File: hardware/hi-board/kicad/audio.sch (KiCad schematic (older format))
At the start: 10 parts, among them J2 Speaker, U1 LM386

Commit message: Complete display schematic and change footprints
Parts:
- C2, C3: footprint Capacitor_SMD:C_0402_1005Metric -> Capacitor_SMD:C_0603_1608Metric
- R1, R2, R3, R4, R5: footprint Resistor_SMD:R_0402_1005Metric -> Resistor_SMD:R_0603_1608Metric
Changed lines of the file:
@@
 F 0 "R1" V 3400 2950 50  0000 C CNN
 F 1 "1k" V 3400 3150 50  0000 C CNN
-F 2 "Resistor_SMD:R_0402_1005Metric" H 3500 3050 50  0001 C CNN
+F 2 "Resistor_SMD:R_0603_1608Metric" H 3500 3050 50  0001 C CNN
 F 3 "~" H 3500 3050 50  0001 C CNN
 	1    3500 3050
@@
 F 0 "R2" V 3400 3300 50  0000 C CNN
 F 1 "1k" V 3400 3500 50  0000 C CNN
-F 2 "Resistor_SMD:R_0402_1005Metric" H 3500 3400 50  0001 C CNN
+F 2 "Resistor_SMD:R_0603_1608Metric" H 3500 3400 50  0001 C CNN
 F 3 "~" H 3500 3400 50  0001 C CNN
 	1    3500 3400
@@
 F 0 "C2" H 3992 3696 50  0000 L CNN
 F 1 "4.7nF" H 3992 3605 50  0000 L CNN
-F 2 "Capacitor_SMD:C_0402_1005Metric" H 3900 3650 50  0001 C CNN
+F 2 "Capacitor_SMD:C_0603_1608Metric" H 3900 3650 50  0001 C CNN
 F 3 "~" H 3900 3650 50  0001 C CNN
 	1    3900 3650
@@
 F 0 "R3" V 4600 3300 50  0000 C CNN
 F 1 "10k" V 4600 3500 50  0000 C CNN
-F 2 "Resistor_SMD:R_0402_1005Metric" H 4700 3400 50  0001 C CNN
+F 2 "Resistor_SMD:R_0603_1608Metric" H 4700 3400 50  0001 C CNN
 F 3 "~" H 4700 3400 50  0001 C CNN
 	1    4700 3400
@@
 F 0 "R4" H 4359 3696 50  0000 L CNN
 F 1 "4.7k" H 4359 3605 50  0000 L CNN
-F 2 "Resistor_SMD:R_0402_1005Metric" H 4300 3650 50  0001 C CNN
+F 2 "Resistor_SMD:R_0603_1608Metric" H 4300 3650 50  0001 C CNN
 F 3 "~" H 4300 3650 50  0001 C CNN
 	1    4300 3650
@@
 F 0 "C3" H 6092 3696 50  0000 L CNN
 F 1 "47nF" H 6092 3605 50  0000 L CNN
-F 2 "Capacitor_SMD:C_0402_1005Metric" H 6000 3650 50  0001 C CNN
+F 2 "Capacitor_SMD:C_0603_1608Metric" H 6000 3650 50  0001 C CNN
 F 3 "~" H 6000 3650 50  0001 C CNN
 	1    6000 3650
@@
 F 0 "R5" H 6059 3946 50  0000 L CNN
 F 1 "10Ω" H 6059 3855 50  0000 L CNN
-F 2 "Resistor_SMD:R_0402_1005Metric" H 6000 3900 50  0001 C CNN
+F 2 "Resistor_SMD:R_0603_1608Metric" H 6000 3900 50  0001 C CNN
 F 3 "~" H 6000 3900 50  0001 C CNN
 	1    6000 3900

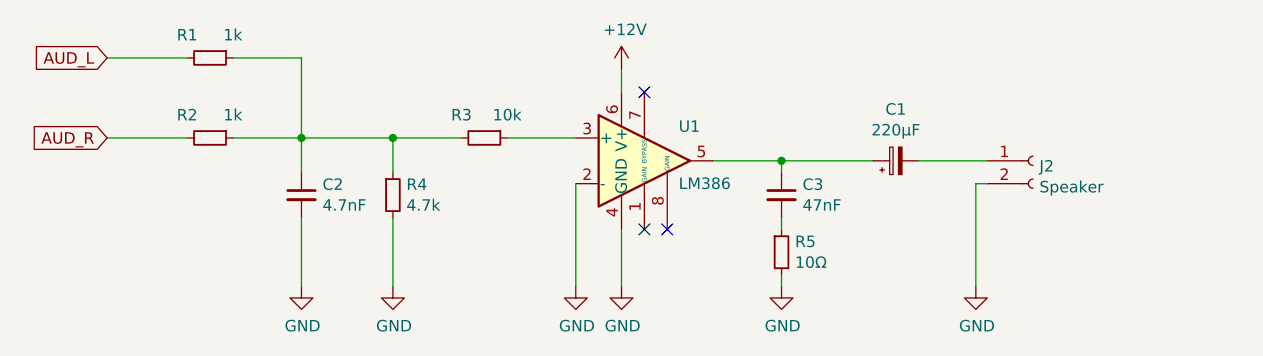
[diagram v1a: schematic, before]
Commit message: Update audio circuit to SMD only
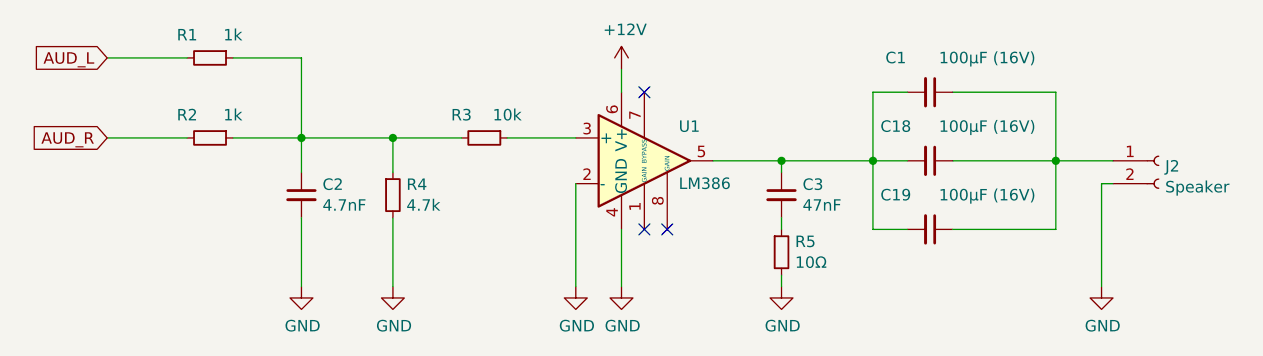
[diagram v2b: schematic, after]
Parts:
- removed C1: 220µF, Capacitor_THT:CP_Radial_D6.3mm_P2.50mm, symbol Device:CP_Small
- added C1, C18, C19: 100µF (16V), Capacitor_SMD:C_1210_3225Metric, symbol Device:C_Small
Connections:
- net at C3.1, U1.5: now also C1.2, C18.2, C19.2
- net at J2.1 (Pin_1): now also C1.1, C18.1, C19.1
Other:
- moved on the sheet: J2
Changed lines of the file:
@@
 Wire Wire Line
 	6000 3500 5700 3500
-$Comp
-L Device:CP_Small C1
-U 1 1 6141A883
-P 6500 3500
-F 0 "C1" V 6725 3500 50  0000 C CNN
-F 1 "220µF" V 6634 3500 50  0000 C CNN
-F 2 "Capacitor_THT:CP_Radial_D6.3mm_P2.50mm" H 6500 3500 50  0001 C CNN
-F 3 "~" H 6500 3500 50  0001 C CNN
-	1    6500 3500
-	0    -1   -1   0
-$EndComp
-Wire Wire Line
-	6000 3500 6400 3500
 Connection ~ 6000 3500
 $Comp
 L Connector:Conn_01x02_Female J2
 U 1 1 6141BB60
-P 7100 3500
-F 0 "J2" H 7128 3476 50  0000 L CNN
-F 1 "Speaker" H 7128 3385 50  0000 L CNN
-F 2 "Connector_PinHeader_2.54mm:PinHeader_1x02_P2.54mm_Vertical" H 7100 3500 50  0001 C CNN
-F 3 "~" H 7100 3500 50  0001 C CNN
-	1    7100 3500
+P 7650 3500
+F 0 "J2" H 7678 3476 50  0000 L CNN
+F 1 "Speaker" H 7678 3385 50  0000 L CNN
+F 2 "Connector_PinHeader_2.54mm:PinHeader_1x02_P2.54mm_Vertical" H 7650 3500 50  0001 C CNN
+F 3 "~" H 7650 3500 50  0001 C CNN
+	1    7650 3500
 	1    0    0    -1
 $EndComp
 Wire Wire Line
-	6600 3500 6900 3500
+	7450 3600 7400 3600
 Wire Wire Line
-	6900 3600 6850 3600
-Wire Wire Line
-	6850 3600 6850 4050
+	7400 3600 7400 4050
 $Comp
 L power:GND #PWR0118
 U 1 1 6141CFCA
-P 6850 4050
-F 0 "#PWR0118" H 6850 3800 50  0001 C CNN
-F 1 "GND" H 6855 3877 50  0000 C CNN
-F 2 "" H 6850 4050 50  0001 C CNN
-F 3 "" H 6850 4050 50  0001 C CNN
-	1    6850 4050
+P 7400 4050
+F 0 "#PWR0118" H 7400 3800 50  0001 C CNN
+F 1 "GND" H 7405 3877 50  0000 C CNN
+F 2 "" H 7400 4050 50  0001 C CNN
+F 3 "" H 7400 4050 50  0001 C CNN
+	1    7400 4050
 	1    0    0    -1
 $EndComp
+$Comp
+L Device:C_Small C1
+U 1 1 6162E602
+P 6650 3200
+F 0 "C1" V 6500 3050 50  0000 C CNN
+F 1 "100µF (16V)" V 6500 3450 50  0000 C CNN
+F 2 "Capacitor_SMD:C_1210_3225Metric" H 6650 3200 50  0001 C CNN
+F 3 "~" H 6650 3200 50  0001 C CNN
+	1    6650 3200
+	0    1    1    0
+$EndComp
+$Comp
+L Device:C_Small C18
+U 1 1 6162F09A
+P 6650 3500
+F 0 "C18" V 6500 3350 50  0000 C CNN
+F 1 "100µF (16V)" V 6500 3750 50  0000 C CNN
+F 2 "Capacitor_SMD:C_1210_3225Metric" H 6650 3500 50  0001 C CNN
+F 3 "~" H 6650 3500 50  0001 C CNN
+	1    6650 3500
+	0    1    1    0
+$EndComp
+$Comp
+L Device:C_Small C19
+U 1 1 6162F4E5
+P 6650 3800
+F 0 "C19" V 6500 3650 50  0000 C CNN
+F 1 "100µF (16V)" V 6500 4050 50  0000 C CNN
+F 2 "Capacitor_SMD:C_1210_3225Metric" H 6650 3800 50  0001 C CNN
+F 3 "~" H 6650 3800 50  0001 C CNN
+	1    6650 3800
+	0    1    1    0
+$EndComp
+Wire Wire Line
+	6000 3500 6400 3500
+Wire Wire Line
+	6400 3500 6400 3200
+Wire Wire Line
+	6400 3200 6550 3200
+Connection ~ 6400 3500
+Wire Wire Line
+	6400 3500 6550 3500
+Wire Wire Line
+	6400 3500 6400 3800
+Wire Wire Line
+	6400 3800 6550 3800
+Wire Wire Line
+	6750 3500 7200 3500
+Wire Wire Line
+	6750 3800 7200 3800
+Wire Wire Line
+	7200 3800 7200 3500
+Connection ~ 7200 3500
+Wire Wire Line
+	7200 3500 7450 3500
+Wire Wire Line
+	6750 3200 7200 3200
+Wire Wire Line
+	7200 3200 7200 3500
 $EndSCHEMATC
